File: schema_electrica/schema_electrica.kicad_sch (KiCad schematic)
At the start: 13 parts, among them M1 Motor_DC, M2 Motor_DC, M3 Motor_DC, M4 Motor_DC, SW1 SW_DIP_x01, U1 L298N, U2 DHT11

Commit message: actualizare schema
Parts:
- removed HC-SR04: ~, symbol Arduino_Components:HC-SR04
- removed MQ-135: ~, symbol Arduino_Components:MQ-135
- added DS1302: ~, symbol ArduinoComponents:DS1302
- added LCD-1602-I2C: ~, symbol ArduinoComponents:LCD_1602_I2C
- added MQ-135: ~, symbol ArduinoComponents:MQ-135
- added MicroSDCardAdapter: ~, symbol ArduinoComponents:Micro_SD_Card_Adapter
- added UVSensor1: ~, symbol ArduinoComponents:UV_Sensor
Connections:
- net +5V: now also DS1302.1 (VCC), LCD-1602-I2C.1 (VCC), MQ-135.1 (VCC), MicroSDCardAdapter.1 (VCC), UVSensor1.1 (VCC)
- net GND: now also DS1302.5 (GND), LCD-1602-I2C.4 (GND), MQ-135.4 (GND), MicroSDCardAdapter.6 (GND), UVSensor1.3 (GND)
- net at A1.26 (D11): now also MicroSDCardAdapter.4 (MOSI)
- net at A1.25 (D10): now also DS1302.2 (CLK)
- net at A1.9 (A0): now also MQ-135.3 (AO)
- net at A1.13 (SDA/A4): now also LCD-1602-I2C.2 (SDA); no longer BMP-180.2 (SDA)
- net at A1.14 (SCL/A5): now also LCD-1602-I2C.3 (SCL); no longer BMP-180.3 (SCL)
- net at A1.10 (A1): now also UVSensor1.2 (OUT)
- net at A1.17 (D2): now also MicroSDCardAdapter.2 (CS)
- net at A1.23 (D8): now also DS1302.4 (RST)
- net at A1.24 (D9): now also DS1302.3 (DAT)
- net at A1.27 (D12): now also MicroSDCardAdapter.5 (MISO)
- net at A1.28 (D13): now also MicroSDCardAdapter.3 (SCK)
- net at A1.31 (SDA/A4): now also BMP-180.2 (SDA)
- net at A1.32 (SCL/A5): now also BMP-180.3 (SCL)
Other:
- moved on the sheet: A1, BMP-180, BT1, HC-05, M1, M2, M3, M4, SW1, U1, U2

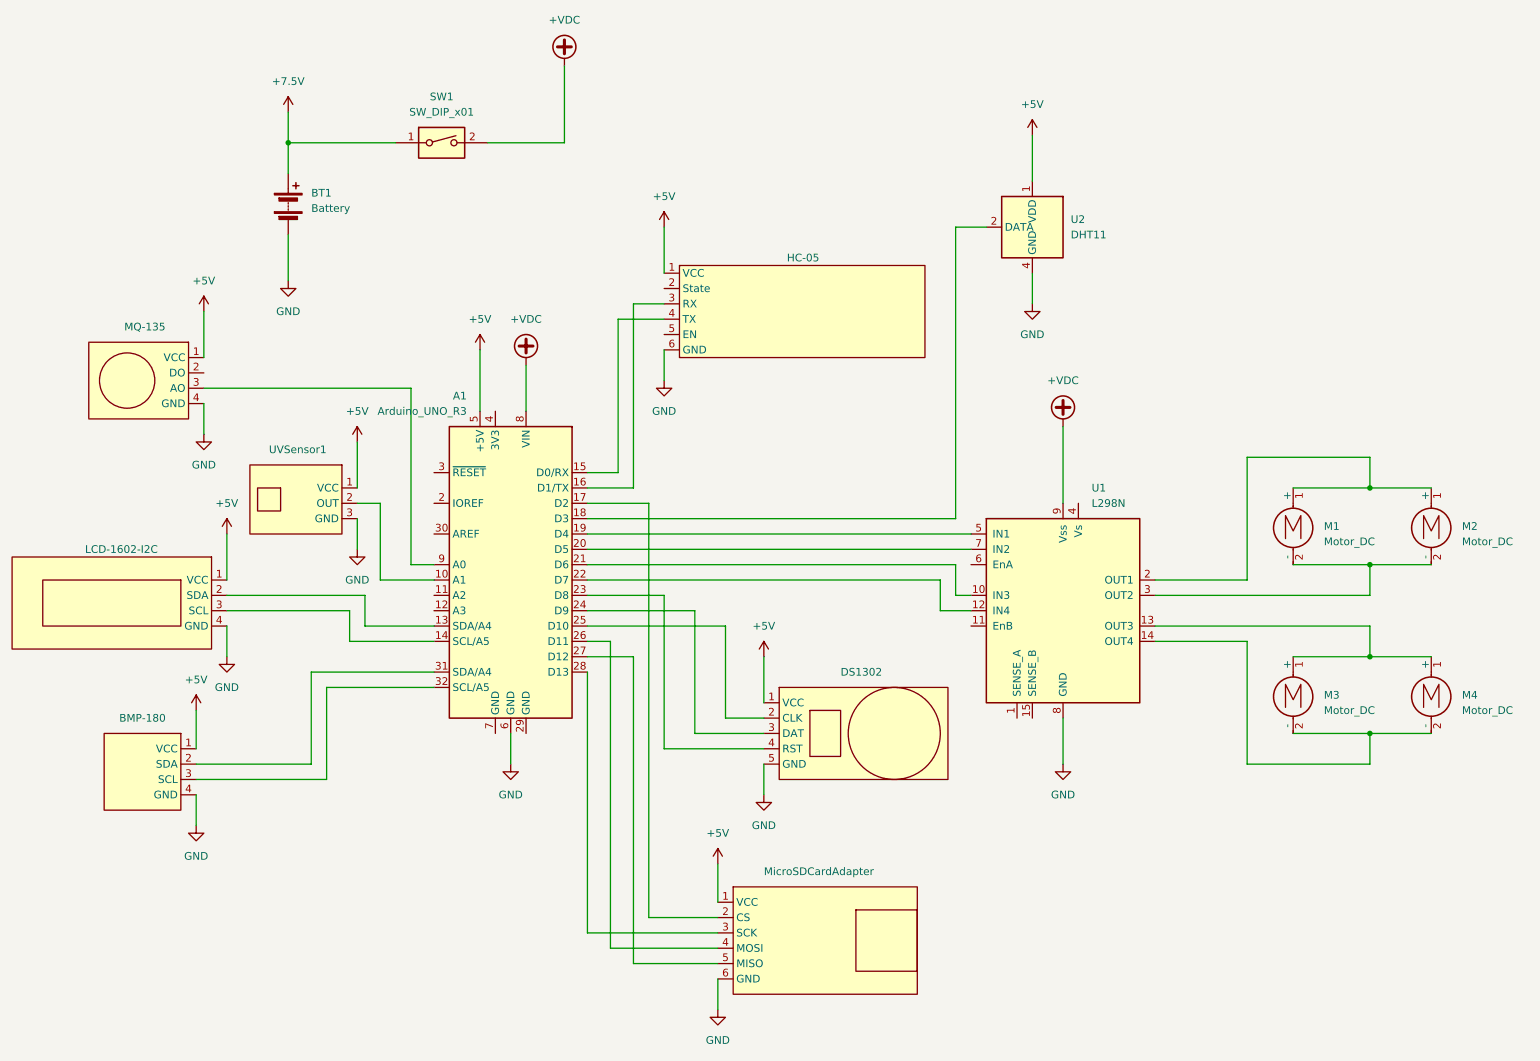
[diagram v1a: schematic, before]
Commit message: actualizare schema electrica
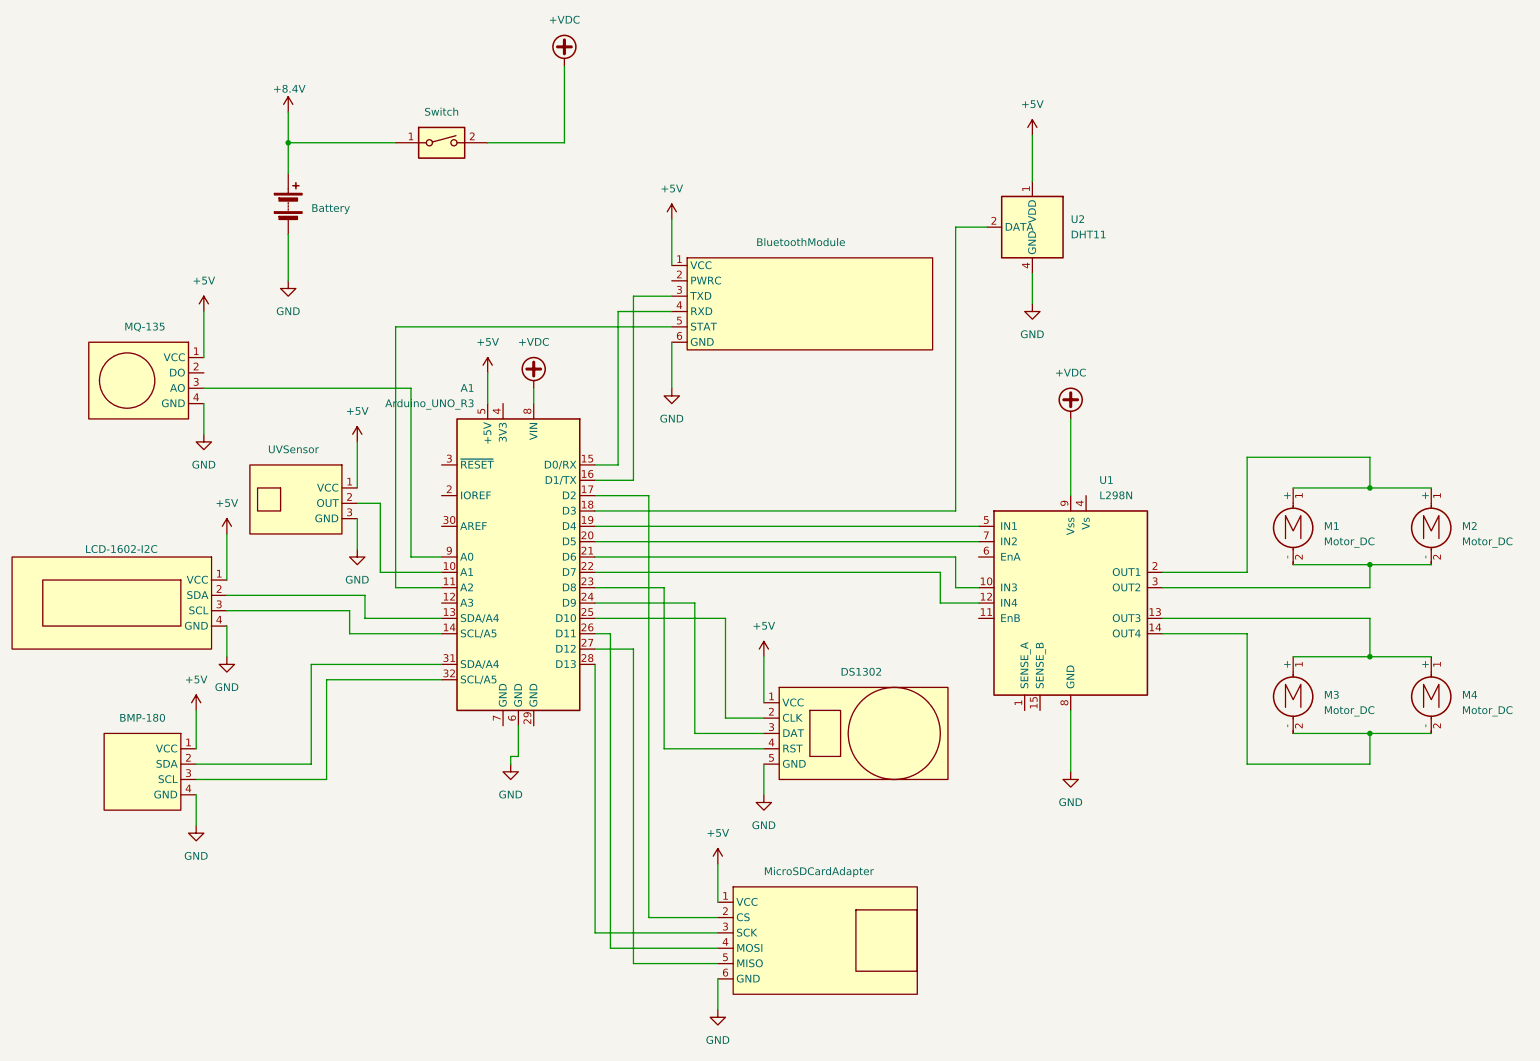
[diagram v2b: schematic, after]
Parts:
- removed HC-05: ~, symbol Arduino_Components:HC-05
- added +8.4V: ~, symbol power2:+8.4V
- added BluetoothModule: ~, symbol Arduino_Components:Bluetooth_Module
- SW1: value SW_DIP_x01 -> Switch
- renumbered UVSensor1 to UVSensor
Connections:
- net +5V: now also BluetoothModule.1 (VCC)
- net GND: now also BluetoothModule.6 (GND)
- net at A1.16 (D1/TX): now also BluetoothModule.3 (TXD)
- net at A1.15 (D0/RX): now also BluetoothModule.4 (RXD)
- net at A1.11 (A2): now also BluetoothModule.5 (STAT)
- net +7.5V renamed +8.4V
- net +8.4V: now also +8.4V.1 (+8.4V)
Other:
- moved on the sheet: A1, U1
